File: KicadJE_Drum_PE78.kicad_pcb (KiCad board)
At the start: 2 copper layers, 183 x 128 mm, 156 parts, among them J101 Snare, J102 LCymbals, J103 SCymbals, J104 Maracas, J105 Bass, J106 LBongo, J107 HBongo, J108 Claves, J201 AudioJack2_SwitchT, J202 AudioJack2_SwitchT, J203 AudioJack2_SwitchT, J204 Power +, J205 Power -, J206 Conn_01x03_Male, J207 Conn_01x03_Male, J208 Conn_01x03_Male, J209 Conn_01x03_Male, J210 Conn_01x02_Male, J301 Tone/Noise, J302 RND, J303 TONE, J304 DRUM_OUT, J305 Tones, J306 Noise, P101 HEADER_2x8_Doepfer, P201 HEADER_2x5_Doepfer, Q101 2N3904, Q102 2N3904, Q103 2N3904, Q104 2N3904, SW201 SW_SPDT, U101 74HC04, U302 TL072

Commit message: BB Power
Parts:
- D201: value On LED -> + On LED
- D202: value On LED -> - On LED
- moved J207 67.5 mm to (87.5, 131.5)
- moved SW201 63.0 mm to (54.0, 113.0)
- moved J209 52.2 mm to (87.0, 67.0)
- moved G*** 44.4 mm to (87.5, 95.0), turned to 90 degrees
- moved J206 35.8 mm to (87.5, 142.0)
- moved R204 34.1 mm to (69.0, 104.0), turned to 90 degrees
- moved J210 32.9 mm to (87.5, 108.0)
- moved R202 28.9 mm to (53.0, 104.0), turned to 90 degrees
- moved J208 28.1 mm to (57.5, 131.0), turned to 270 degrees
- moved R201 25.8 mm to (53.0, 86.0), turned to 270 degrees
- moved J205 24.2 mm to (86.5, 122.5), turned to 270 degrees
- moved D202 19.1 mm to (53.0, 100.0), turned to 270 degrees
- moved R203 17.6 mm to (69.0, 86.0), turned to 270 degrees
- moved D201 16.8 mm to (53.0, 90.0), turned to 90 degrees
- moved D203 16.7 mm to (79.5, 79.2), turned to 270 degrees
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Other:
- board text added: "BB-Power"
- board text added: "KicadJE-BB-Power Johansen Engineering 22/4/2021 Rev A"

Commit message: Powerfootprintupdated
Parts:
- added C101: 330n, AJ:C_0805_AJ, F.Cu at (155.6, 27.8)
- added C102: 100n, AJ:C_0805_AJ, F.Cu at (169.9, 16.0)
- added C103: 220n, AJ:C_0805_AJ, F.Cu at (165.1, 18.9)
- added C104: 150n, AJ:C_0805_AJ, F.Cu at (160.4, 21.9)
- added C105: 47n, AJ:C_0805_AJ, F.Cu at (155.6, 24.8)
- added C106: 68n, AJ:C_0805_AJ, F.Cu at (165.1, 16.0)
- added C107: 100n, AJ:C_0805_AJ, F.Cu at (150.9, 27.8)
- added C108: 68n, AJ:C_0805_AJ, F.Cu at (160.4, 18.9)
- added C109: 47n, AJ:C_0805_AJ, F.Cu at (155.6, 21.9)
- added C110: 15n, AJ:C_0805_AJ, F.Cu at (150.9, 24.8)
- added C111: 4n7, AJ:C_0805_AJ, F.Cu at (160.4, 16.0)
- added C112: 4n7, AJ:C_0805_AJ, F.Cu at (155.6, 18.9)
- added C113: 150n, AJ:C_0805_AJ, F.Cu at (150.9, 21.9)
- added C114: 47n, AJ:C_0805_AJ, F.Cu at (155.6, 16.0)
- added C115: 47n, AJ:C_0805_AJ, F.Cu at (150.9, 16.0)
- added C116: 15n, AJ:C_0805_AJ, F.Cu at (150.9, 18.9)
- added C117: 22n, AJ:C_0805_AJ, F.Cu at (160.4, 24.8)
- added C118: 33n, AJ:C_0805_AJ, F.Cu at (165.1, 21.9)
- added C119: 4n7, AJ:C_0805_AJ, F.Cu at (169.9, 18.9)
- added C120: 100n, AJ:C_0805_AJ, F.Cu at (160.4, 27.8)
- added C121: 10n, AJ:C_0805_AJ, F.Cu at (174.6, 16.0)
- added C122: 1n5, AJ:C_0805_AJ, F.Cu at (165.1, 24.8)
- added C123: 33n, AJ:C_0805_AJ, F.Cu at (169.9, 21.9)
- added C124: 4n7, AJ:C_0805_AJ, F.Cu at (174.6, 18.9)
- added C125: 10n, AJ:C_0805_AJ, F.Cu at (165.1, 27.8)
- added C126: 1n5, AJ:C_0805_AJ, F.Cu at (169.9, 24.8)
- added C127: 1u, AJ:C_0805_AJ, F.Cu at (174.6, 21.9)
- added C128: 1u, AJ:C_0805_AJ, F.Cu at (169.9, 27.8)
- added C129: 1u, AJ:C_0805_AJ, F.Cu at (174.6, 24.8)
- added C130: 100n, AJ:C_0805_AJ, F.Cu at (174.6, 27.8)
- added C201: 1u, AJ:C_0805_AJ, F.Cu at (79.5, 79.0)
- added C202: 1u, AJ:C_0805_AJ, F.Cu at (79.5, 124.0)
- added C301: 4n7, AJ:C_0805_AJ, F.Cu at (183.9, 24.8)
- added C302: 4n7, AJ:C_0805_AJ, F.Cu at (188.7, 24.8)
- added C303: 220n, AJ:C_0805_AJ, B.Cu at (62.0, 174.5)
- D201: value + On LED -> On LED
- D202: value - On LED -> On LED
- RV102: value R_POT -> 220k
- moved RV101 80.0 mm to (158.5, 99.0)
- moved J306 64.9 mm to (164.5, 112.5)
- moved R110 45.3 mm to (139.9, 183.4)
- moved R128 45.3 mm to (130.4, 183.0)
- moved R148 45.3 mm to (135.2, 183.3)
- moved R130 45.3 mm to (125.7, 183.0)
- moved R112 43.7 mm to (128.4, 187.9)
- moved R125 43.7 mm to (133.1, 188.2)
- moved R145 43.7 mm to (137.9, 188.4)
- moved R101 39.1 mm to (125.5, 193.7)
- moved R107 39.1 mm to (139.7, 193.3)
- moved R118 39.1 mm to (130.2, 193.8)
- moved R129 39.1 mm to (135.0, 193.8)
- moved R139 38.3 mm to (139.7, 197.2)
- moved L103 36.3 mm to (127.5, 204.5)
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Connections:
- P101 pad 1: (no net) -> Net-(D109-Pad1)
- P101 pad 10: (no net) -> Net-(P101-Pad10)
- P101 pad 11: (no net) -> Net-(P101-Pad11)
- P101 pad 12: (no net) -> Net-(P101-Pad11)
- P101 pad 13: (no net) -> Net-(P101-Pad13)
- P101 pad 14: (no net) -> Net-(P101-Pad14)
- P101 pad 15: (no net) -> Net-(P101-Pad15)
- P101 pad 16: (no net) -> Net-(P101-Pad16)
- P101 pad 2: (no net) -> Net-(D109-Pad1)
- P101 pad 3: (no net) -> GND
- P101 pad 4: (no net) -> GND
- P101 pad 5: (no net) -> GND
- P101 pad 6: (no net) -> GND
- P101 pad 7: (no net) -> GND
- P101 pad 8: (no net) -> GND
- P101 pad 9: (no net) -> Net-(P101-Pad10)
- R146 pad 2: Net-(P101-Pad+5) -> Net-(P101-Pad11)
- R151 pad 2: Net-(P101-Pad+12) -> Net-(P101-Pad10)
- R316 pad 1: Net-(R316-Pad1) -> Net-(R313-Pad2)

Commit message: 3D upd
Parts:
- removed RV301: R_POT, AJ:Potentiometer_China_RK09_Single_Vertical_AJ
- C101, C102, C103, C104, C105, C106, C107, C108, C109, C110, C111, C112, C113, C114, C115, C116, C117, C118, C119, C120, C121, C122, C123, C124, C125, C126, C301, C302: moved to B.Cu
- D109, R138, R145, R146, R151: moved to F.Cu
- moved R138 173.0 mm to (136.5, 51.5), turned to 180 degrees
- moved R151 167.8 mm to (131.5, 60.0)
- moved R146 143.0 mm to (136.5, 60.0), turned to 180 degrees
- moved D109 134.7 mm to (132.0, 51.5)
- moved R145 129.1 mm to (124.0, 60.0), turned to 180 degrees
- moved C130 69.6 mm to (149.0, 92.5)
- moved C127 60.3 mm to (131.5, 64.0)
- moved C128 58.5 mm to (124.0, 64.0), turned to 180 degrees
- moved C129 54.6 mm to (136.5, 64.0), turned to 180 degrees
- moved C105 33.9 mm to (124.6, 11.2)
- moved C101 33.6 mm to (124.6, 14.7)
- moved C112 32.9 mm to (124.6, 30.1)
- moved C114 32.7 mm to (124.6, 26.5)
- moved C109 31.0 mm to (124.6, 20.6)
- moved C110 22.6 mm to (132.9, 11.2)
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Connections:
- net Net-(D109-Pad1) renamed /-12
- net Net-(P101-Pad10) renamed /+12
- net Net-(P101-Pad11) renamed /+5

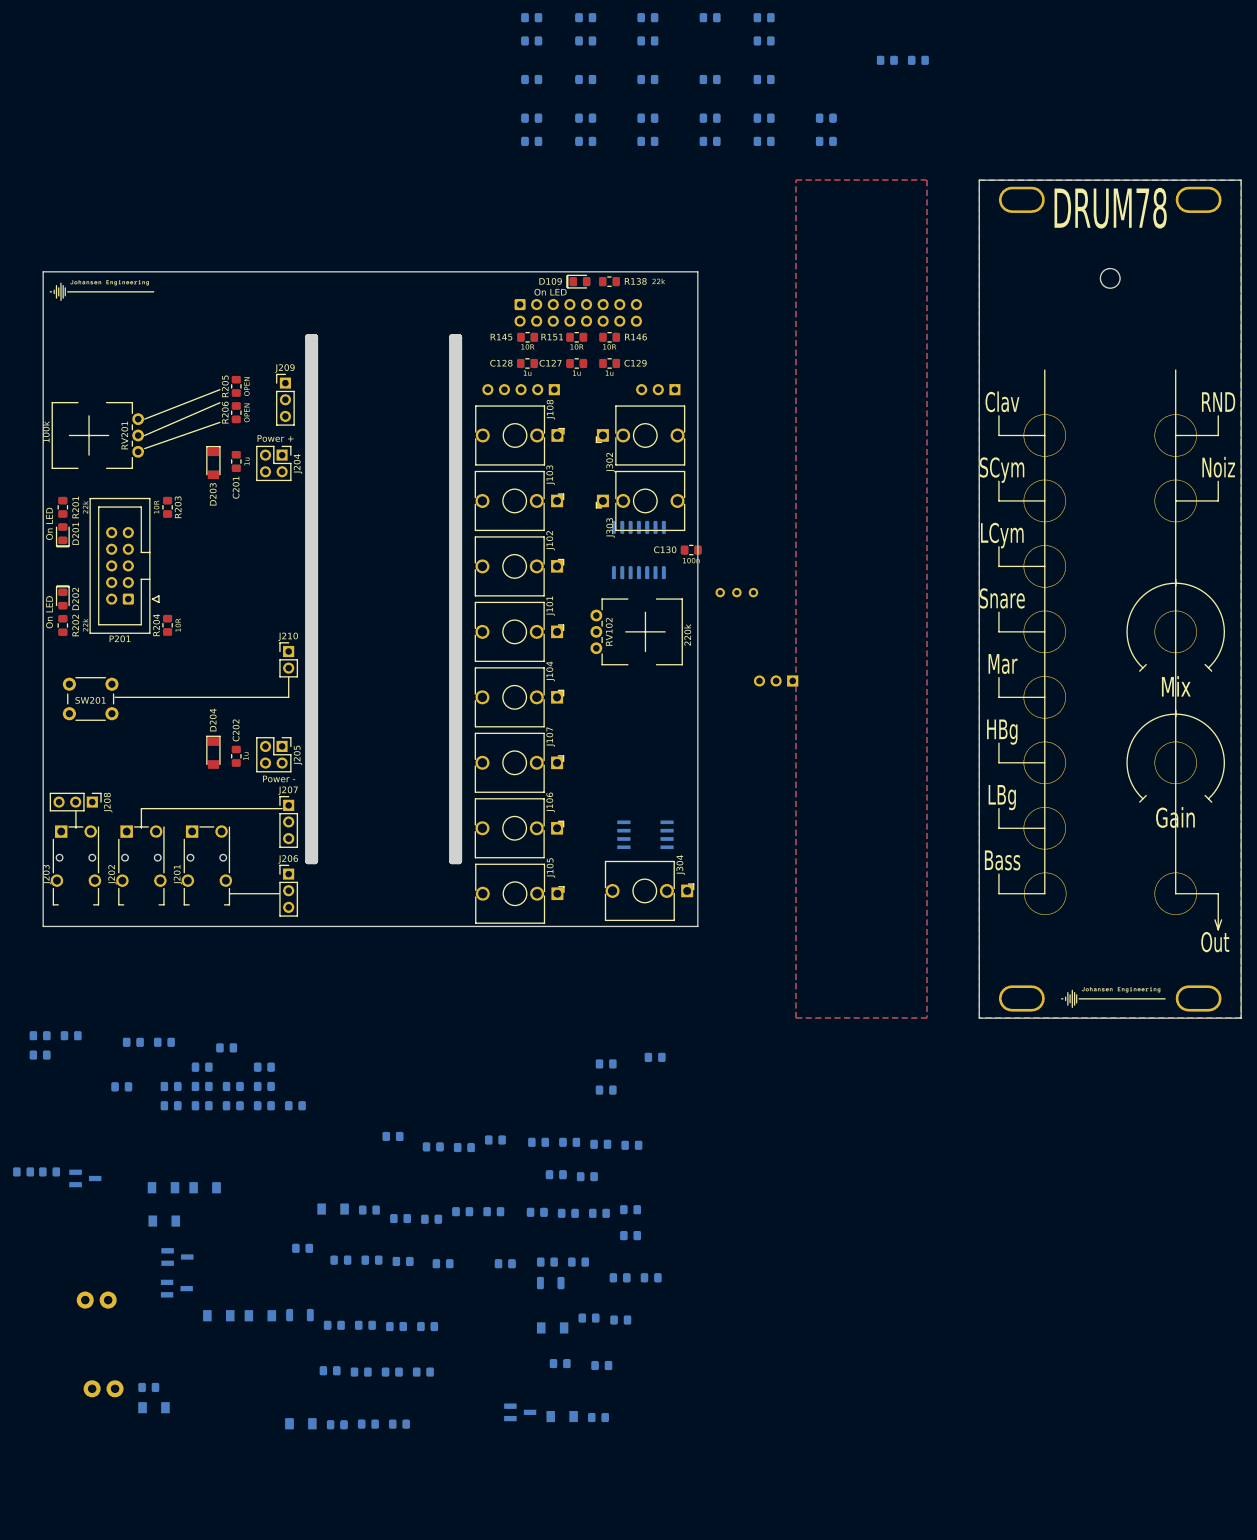
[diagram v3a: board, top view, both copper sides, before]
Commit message: Components initially placed
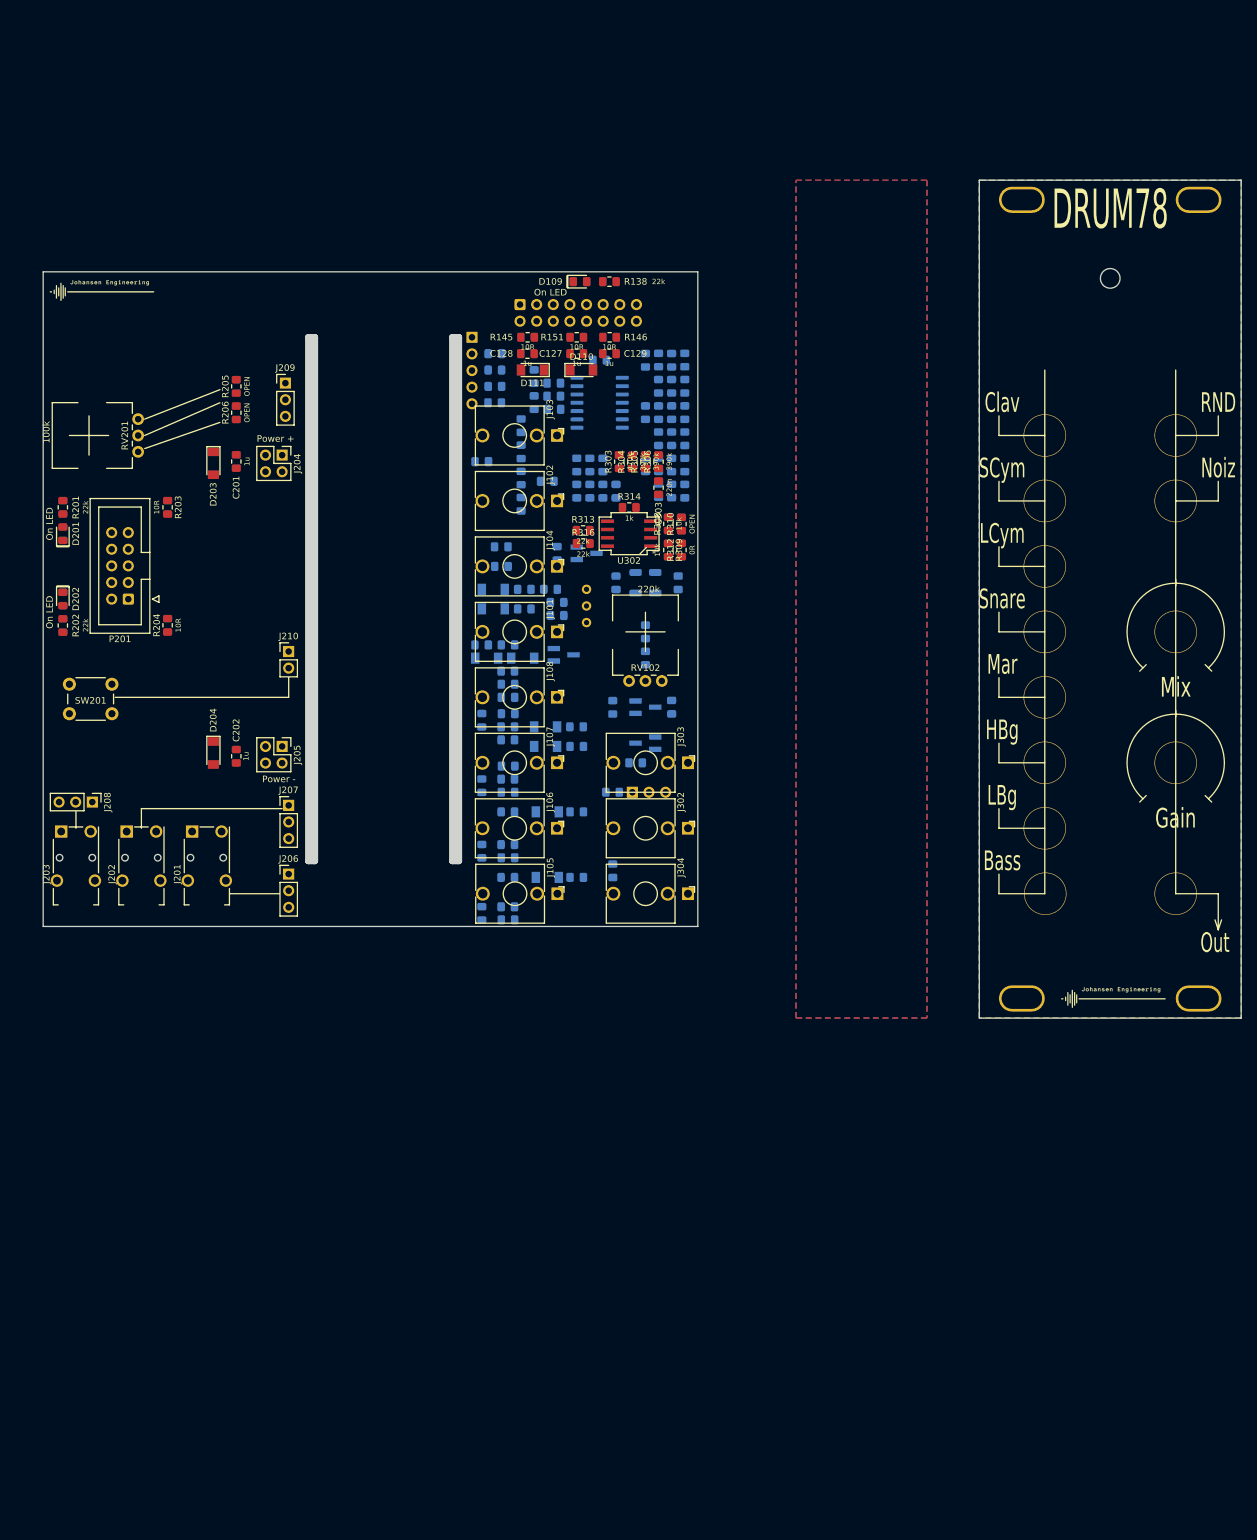
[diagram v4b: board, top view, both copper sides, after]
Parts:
- removed J306: Noise, Connector_PinHeader_2.54mm:PinHeader_1x03_P2.54mm_Vertical
- removed L101, L102: 100mH, Inductor_THT:L_Radial_D7.5mm_P3.50mm_Fastron_07P
- removed R321, R322: 10k, AJ:R_0805_AJ
- added C304: 220n, AJ:C_0805_AJ, B.Cu at (140.5, 125.0)
- C130: moved to B.Cu
- C303, D110, D111, R303, R304, R305, R306, R308, R309, R310, R312, R313, R314, R316, U302: moved to F.Cu
- J303: value TONE -> Noise
- R315: value 0R -> 470r
- moved D110 171.5 mm to (132.2, 65.0)
- moved R122 153.1 mm to (144.0, 79.5), turned to 90 degrees
- moved R103 150.3 mm to (117.0, 79.0), turned to 180 degrees
- moved R147 148.8 mm to (146.0, 75.5), turned to 90 degrees
- moved R119 146.8 mm to (146.0, 63.5), turned to 90 degrees
- moved R120 145.8 mm to (144.0, 63.5), turned to 90 degrees
- moved R143 145.5 mm to (133.5, 83.5), turned to 270 degrees
- moved R126 142.7 mm to (146.0, 83.5), turned to 90 degrees
- moved R312 138.3 mm to (147.5, 92.5), turned to 90 degrees
- moved R310 138.3 mm to (147.5, 88.5), turned to 90 degrees
- moved R121 138.0 mm to (146.0, 79.5), turned to 90 degrees
- moved R109 137.4 mm to (123.0, 81.5), turned to 270 degrees
- moved D111 137.1 mm to (124.8, 65.0), turned to 180 degrees
- moved R141 129.9 mm to (146.0, 71.5), turned to 90 degrees
- moved C104 129.9 mm to (117.0, 148.0), turned to 270 degrees
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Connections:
- J301 pad 2: Net-(J301-Pad2) -> Net-(C304-Pad2)
- J303 pad T: Net-(J301-Pad2) -> Net-(C304-Pad1)
- R315 pad 1: Net-(R315-Pad1) -> Net-(J304-PadT)
- R315 pad 2: Net-(R313-Pad2) -> Net-(R315-Pad2)
- R316 pad 2: Net-(J304-PadT) -> Net-(R315-Pad2)
- U302 pad 4: (no net) -> -12Vc
- U302 pad 7: Net-(J304-PadT) -> Net-(R315-Pad2)
- U302 pad 8: (no net) -> +12Vc

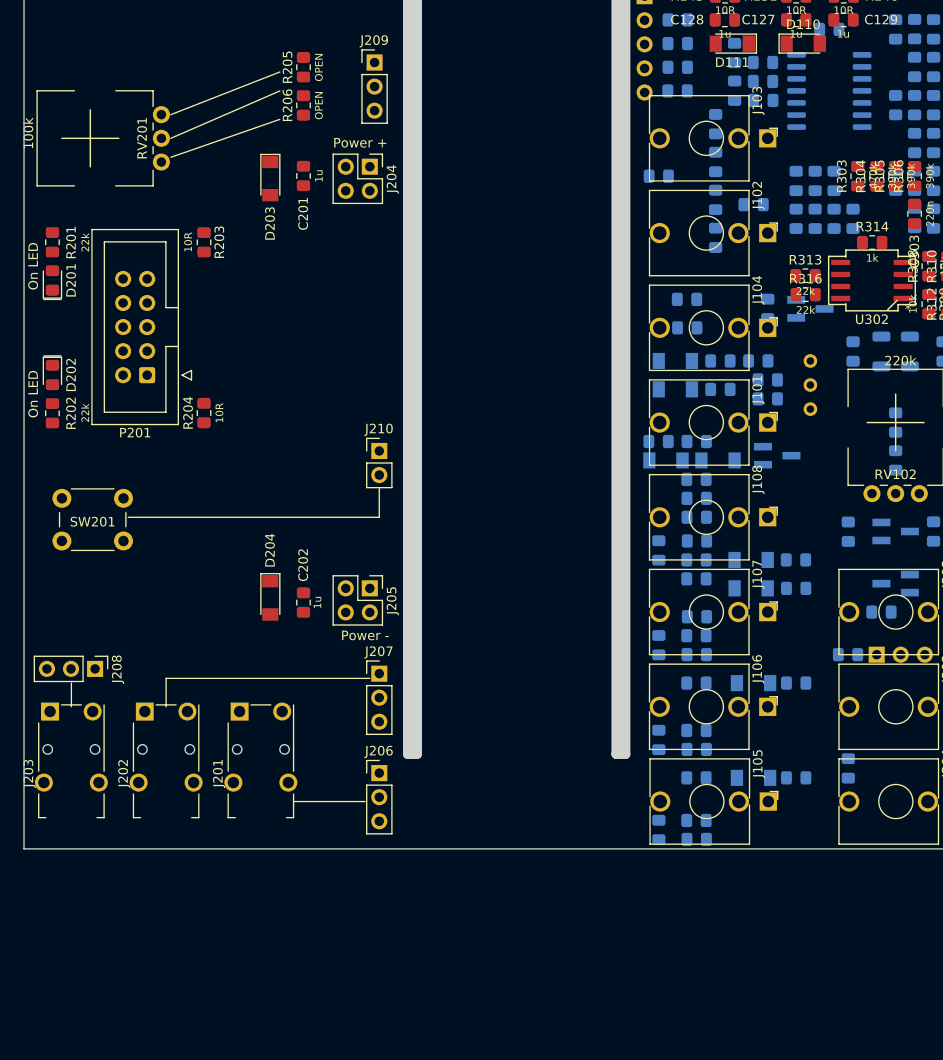
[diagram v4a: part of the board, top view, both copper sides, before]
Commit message: Breadboard routed
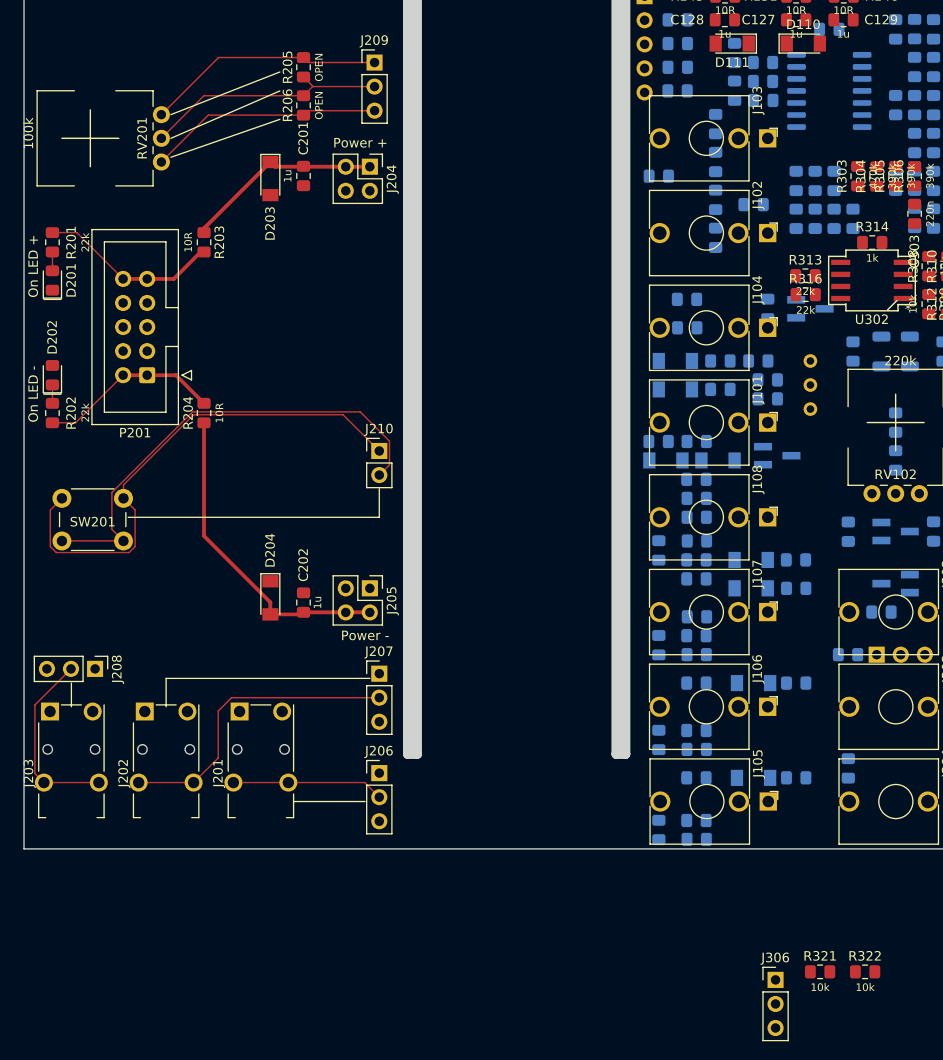
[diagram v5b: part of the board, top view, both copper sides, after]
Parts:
- added J306: Noise, Connector_PinHeader_2.54mm:PinHeader_1x03_P2.54mm_Vertical, F.Cu at (129.3, 163.8)
- added R321: 10k, AJ:R_0805_AJ, F.Cu at (134.0, 163.0)
- added R322: 10k, AJ:R_0805_AJ, F.Cu at (138.8, 163.0)
- D201: value On LED -> On LED +
- D202: value On LED -> On LED -
- turned D202 to 90 degrees
- turned C201 to 270 degrees
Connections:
- net Net-(P201-Pad10) renamed /Breadboard_extender/+12
- D201 pad 1: Net-(D201-Pad1) -> GND
- D202 pad 2: Net-(D201-Pad1) -> GND
- P201 pad 1: Net-(D202-Pad1) -> /Breadboard_extender/-12
- P201 pad 2: Net-(D202-Pad1) -> /Breadboard_extender/-12
- R202 pad 1: GND -> /Breadboard_extender/-12
- R202 pad 2: Net-(D201-Pad1) -> Net-(D202-Pad1)
- R204 pad 2: Net-(D202-Pad1) -> /Breadboard_extender/-12
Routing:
- net Net-(J210-Pad1): track 0.00 -> 53.7 mm
- net Net-(J210-Pad2): track 0.00 -> 50.2 mm
- net -12Vc: track 0.00 -> 33.7 mm
- net Net-(J202-PadT): track 0.00 -> 32.0 mm
- net Net-(J209-Pad2): track 0.00 -> 26.2 mm
- net Net-(J209-Pad1): track 0.00 -> 25.2 mm
- net Net-(J209-Pad3): track 0.00 -> 24.7 mm
- net +12Vc: track 0.00 -> 21.1 mm
- net Net-(J203-PadT): track 0.00 -> 19.8 mm
- net /Breadboard_extender/-12: track 0.00 -> 19.3 mm
- net /Breadboard_extender/+12: track 0.00 -> 19.2 mm
- net Net-(J201-PadT): track 0.00 -> 16.0 mm
- net Net-(D201-Pad2): track 0.00 -> 1.97 mm
- net Net-(D202-Pad1): track 0.00 -> 1.95 mm
